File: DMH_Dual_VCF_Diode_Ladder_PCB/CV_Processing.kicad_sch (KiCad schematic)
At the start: 44 parts, among them SW10 SW_DPDT_OnOn, SW7 SW_SPDT_OnOffOn, SW9 SW_SPDT_OnOffOn, U1 TL074, U2 TL074

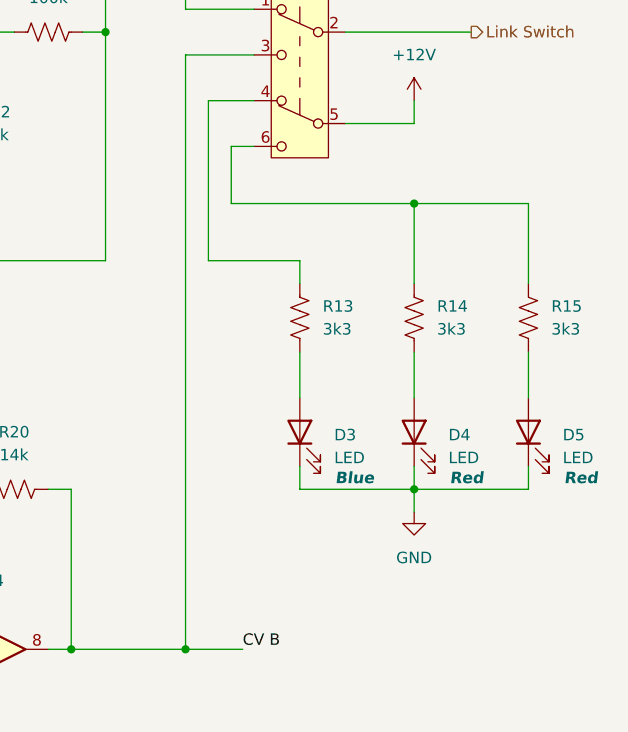
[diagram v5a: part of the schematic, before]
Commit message: Placed location dependent components on PCB
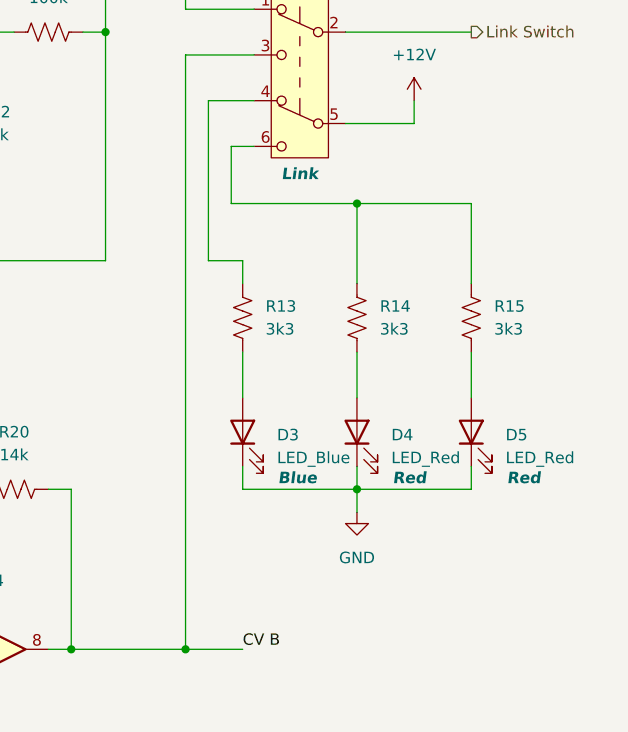
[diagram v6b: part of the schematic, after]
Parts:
- D3: value LED -> LED_Blue
- D4, D5: value LED -> LED_Red
- SW10: Function (none) -> Link
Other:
- moved on the sheet: D3, D4, D5, R13, R14, R15

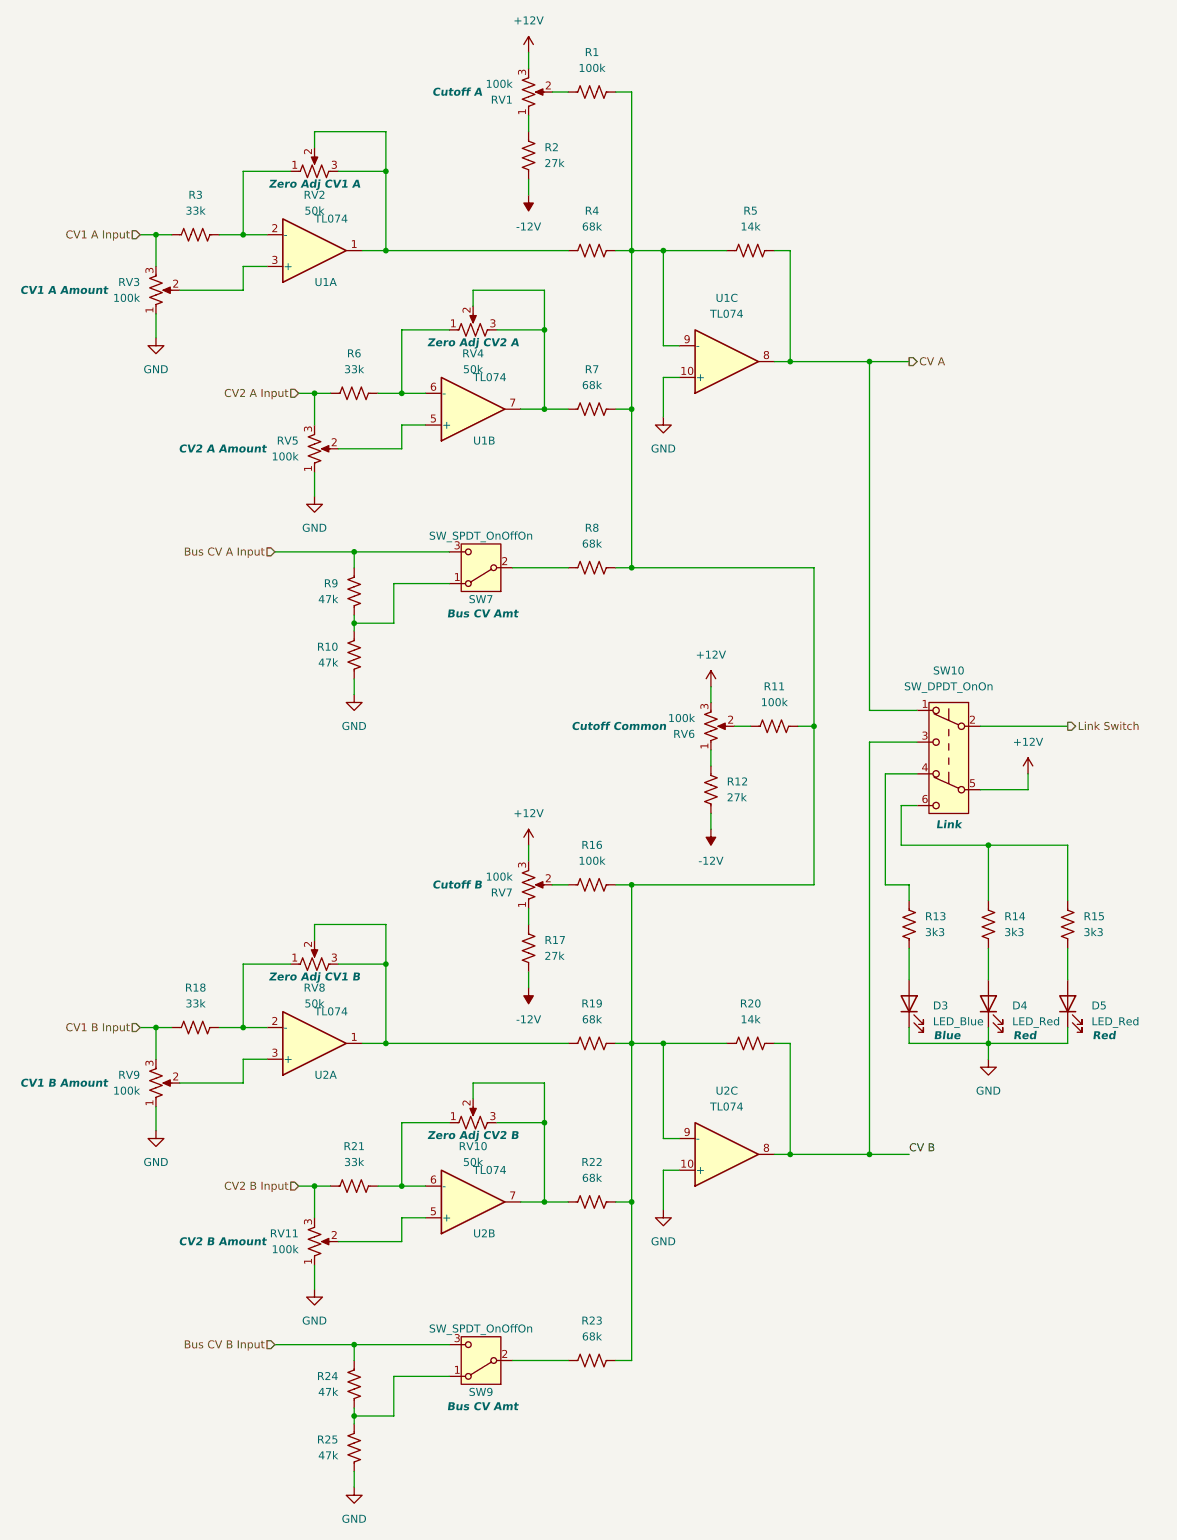
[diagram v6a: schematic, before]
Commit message: Re-annotated OpAmps as per PCB layout
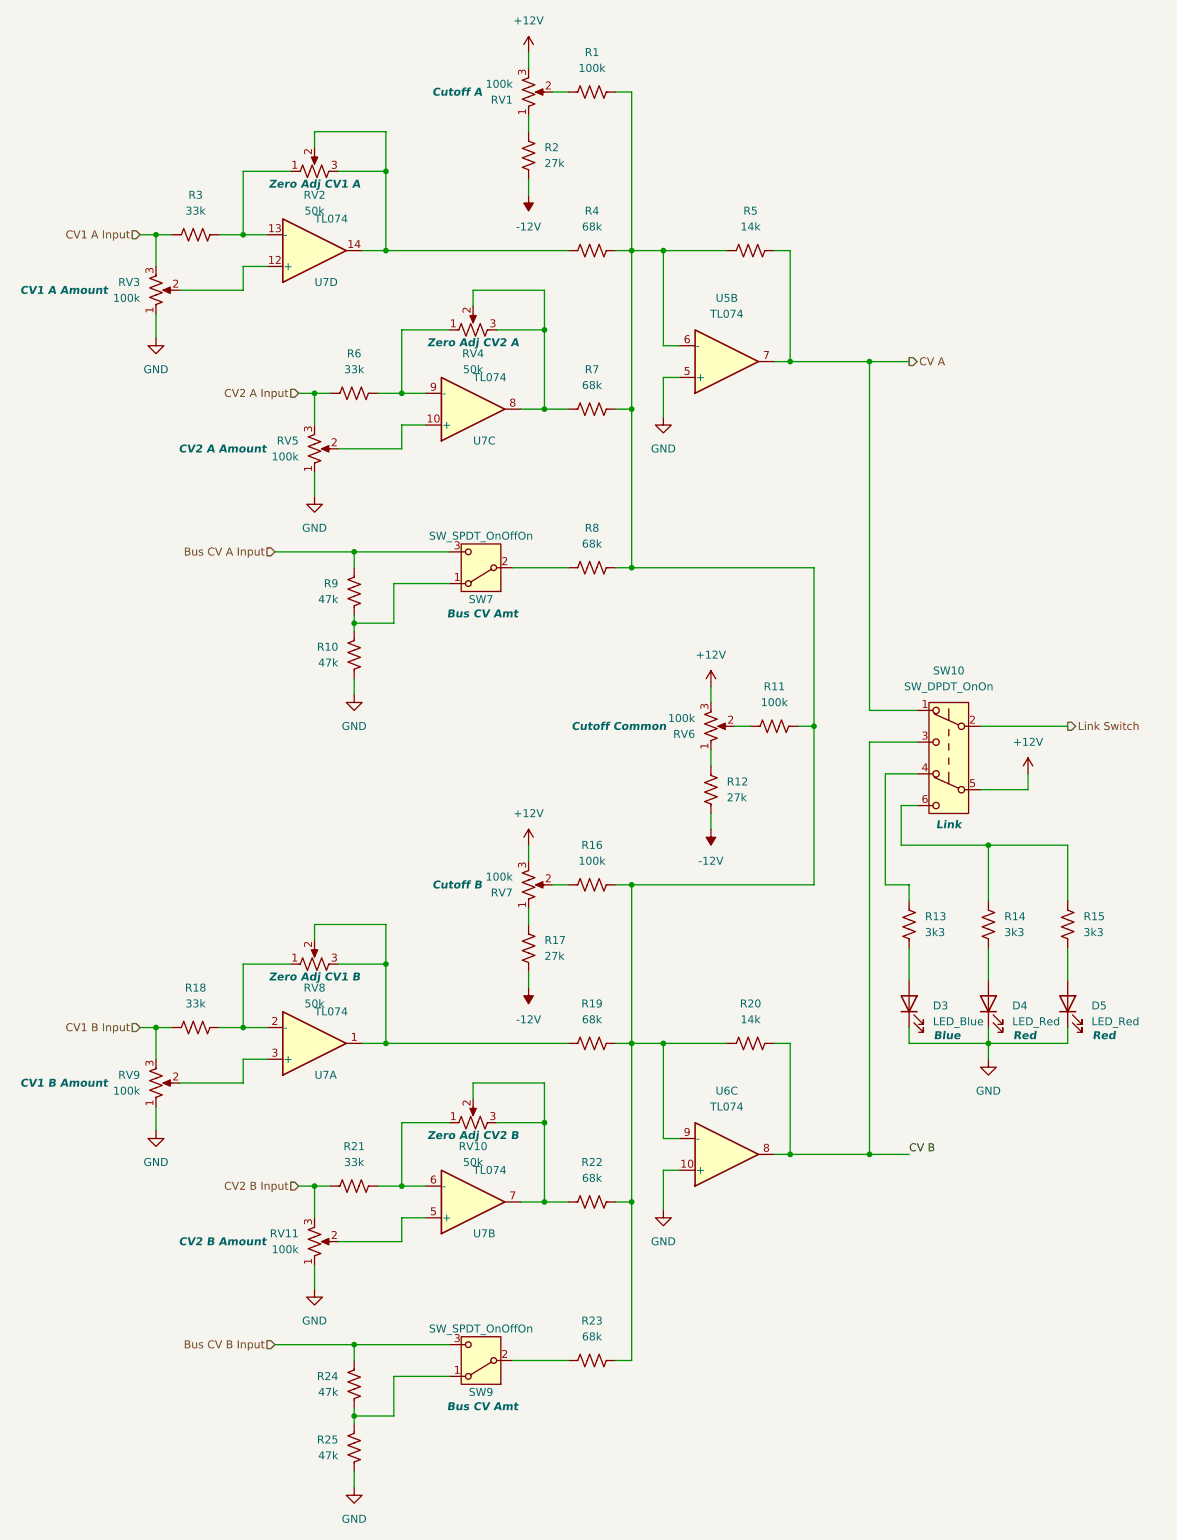
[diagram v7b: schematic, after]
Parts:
- renumbered U1 to U5, U2 to U6, U1 to U7, U2 to U7
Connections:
- net CV A: now also U5.7; no longer U5.8
- net GND: now also U5.5 (+); no longer U5.10 (+)
- net at R1.2, R11.2, R16.2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: now also U5.6 (-); no longer U5.9 (-)
- net at R4.1, RV2.2, RV2.3: now also U7.14; no longer U7.1
- net at R6.2, RV4.1: now also U7.9 (-); no longer U7.6 (-)
- net at R3.2, RV2.1: now also U7.13 (-); no longer U7.2 (-)
- net at RV3.2: now also U7.12 (+); no longer U7.3 (+)
- net at R7.1, RV4.2, RV4.3: now also U7.8; no longer U7.7
- net at RV5.2: now also U7.10 (+); no longer U7.5 (+)
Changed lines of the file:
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@@
 		(dnp no)
 		(fields_autoplaced yes)
-		(property "Reference" "U2"
+		(property "Reference" "U6"
 			(at 129.54 198.12 0)
 			(effects
@@
 			(project "DMH_Dual_VCF_Diode_Ladder_PCB"
 				(path "/58f4306d-5387-4983-bb08-41a2313fd315/ec2d44bc-ed06-4f0b-a22e-df640fa5e089"
-					(reference "U2")
+					(reference "U6")
 					(unit 3)
 				)
@@
 		(at 88.9 88.9 0)
 		(mirror x)
-		(unit 2)
-		(exclude_from_sim no)
-		(in_bom yes)
-		(on_board yes)
-		(dnp no)
-		(property "Reference" "U1"
+		(unit 3)
+		(exclude_from_sim no)
+		(in_bom yes)
+		(on_board yes)
+		(dnp no)
+		(property "Reference" "U7"
 			(at 88.9 93.98 0)
 			(effects
@@
 			(project "DMH_Dual_VCF_Diode_Ladder_PCB"
 				(path "/58f4306d-5387-4983-bb08-41a2313fd315/ec2d44bc-ed06-4f0b-a22e-df640fa5e089"
-					(reference "U1")
-					(unit 2)
+					(reference "U7")
+					(unit 3)
 				)
 			)
@@
 		(on_board yes)
 		(dnp no)
-		(property "Reference" "U2"
+		(property "Reference" "U7"
 			(at 63.5 195.58 0)
 			(effects
@@
 			(project "DMH_Dual_VCF_Diode_Ladder_PCB"
 				(path "/58f4306d-5387-4983-bb08-41a2313fd315/ec2d44bc-ed06-4f0b-a22e-df640fa5e089"
-					(reference "U2")
+					(reference "U7")
 					(unit 1)
 				)
@@
 		(at 129.54 81.28 0)
 		(mirror x)
-		(unit 3)
+		(unit 2)
 		(exclude_from_sim no)
 		(in_bom yes)
@@
 		(dnp no)
 		(fields_autoplaced yes)
-		(property "Reference" "U1"
+		(property "Reference" "U5"
 			(at 129.54 71.12 0)
 			(effects
@@
 			(project "DMH_Dual_VCF_Diode_Ladder_PCB"
 				(path "/58f4306d-5387-4983-bb08-41a2313fd315/ec2d44bc-ed06-4f0b-a22e-df640fa5e089"
-					(reference "U1")
-					(unit 3)
+					(reference "U5")
+					(unit 2)
 				)
 			)
@@
 		(at 63.5 63.5 0)
 		(mirror x)
-		(unit 1)
-		(exclude_from_sim no)
-		(in_bom yes)
-		(on_board yes)
-		(dnp no)
-		(property "Reference" "U1"
+		(unit 4)
+		(exclude_from_sim no)
+		(in_bom yes)
+		(on_board yes)
+		(dnp no)
+		(property "Reference" "U7"
 			(at 63.5 68.58 0)
 			(effects
@@
 			(project "DMH_Dual_VCF_Diode_Ladder_PCB"
 				(path "/58f4306d-5387-4983-bb08-41a2313fd315/ec2d44bc-ed06-4f0b-a22e-df640fa5e089"
-					(reference "U1")
-					(unit 1)
+					(reference "U7")
+					(unit 4)
 				)
 			)
@@
 		(on_board yes)
 		(dnp no)
-		(property "Reference" "U2"
+		(property "Reference" "U7"
 			(at 88.9 220.98 0)
 			(effects
@@
 			(project "DMH_Dual_VCF_Diode_Ladder_PCB"
 				(path "/58f4306d-5387-4983-bb08-41a2313fd315/ec2d44bc-ed06-4f0b-a22e-df640fa5e089"
-					(reference "U2")
+					(reference "U7")
 					(unit 2)
 				)
